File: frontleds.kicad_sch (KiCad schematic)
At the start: 5 parts, among them J13 Conn_02x10_Odd_Even, J5 Conn_02x10_Odd_Even, U18 DMG2305UX-7

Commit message: smol boi
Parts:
- J13, J5: symbol Connector_Generic:Conn_02x10_Counter_Clockwise -> Connector_Generic:Conn_02x10_Odd_Even
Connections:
- net GND: now also J13.1 (Pin_1), J13.3 (Pin_3), J13.5 (Pin_5), J13.7 (Pin_7), J13.9 (Pin_9), J5.11 (Pin_11), J5.13 (Pin_13), J5.15 (Pin_15), J5.17 (Pin_17), J5.19 (Pin_19); no longer J13.12 (Pin_12), J13.14 (Pin_14), J13.16 (Pin_16), J13.18 (Pin_18), J13.20 (Pin_20), J5.10 (Pin_10), J5.2 (Pin_2), J5.4 (Pin_4), J5.6 (Pin_6), J5.8 (Pin_8)
- net LED_1_POW: now also J5.10 (Pin_10), J5.2 (Pin_2), J5.4 (Pin_4), J5.6 (Pin_6), J5.8 (Pin_8); no longer J5.11 (Pin_11), J5.13 (Pin_13), J5.15 (Pin_15), J5.17 (Pin_17), J5.19 (Pin_19)
- net LED_2_POW: now also J13.12 (Pin_12), J13.14 (Pin_14), J13.16 (Pin_16), J13.18 (Pin_18), J13.20 (Pin_20); no longer J13.1 (Pin_1), J13.3 (Pin_3), J13.5 (Pin_5), J13.7 (Pin_7), J13.9 (Pin_9)
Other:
- moved on the sheet: J13

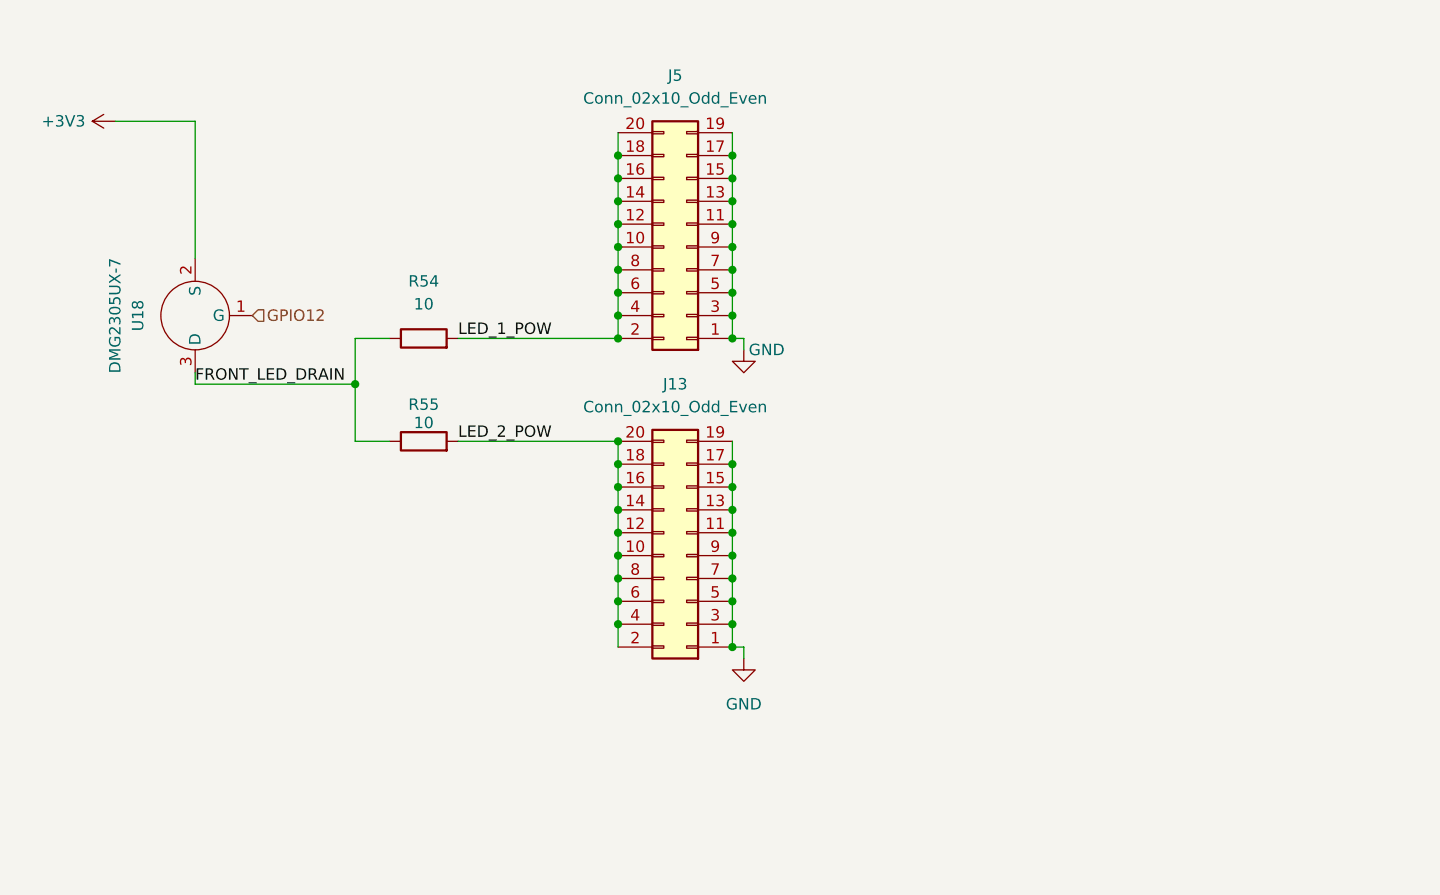
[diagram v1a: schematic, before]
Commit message: changed front leds to use dedicated led current drivers
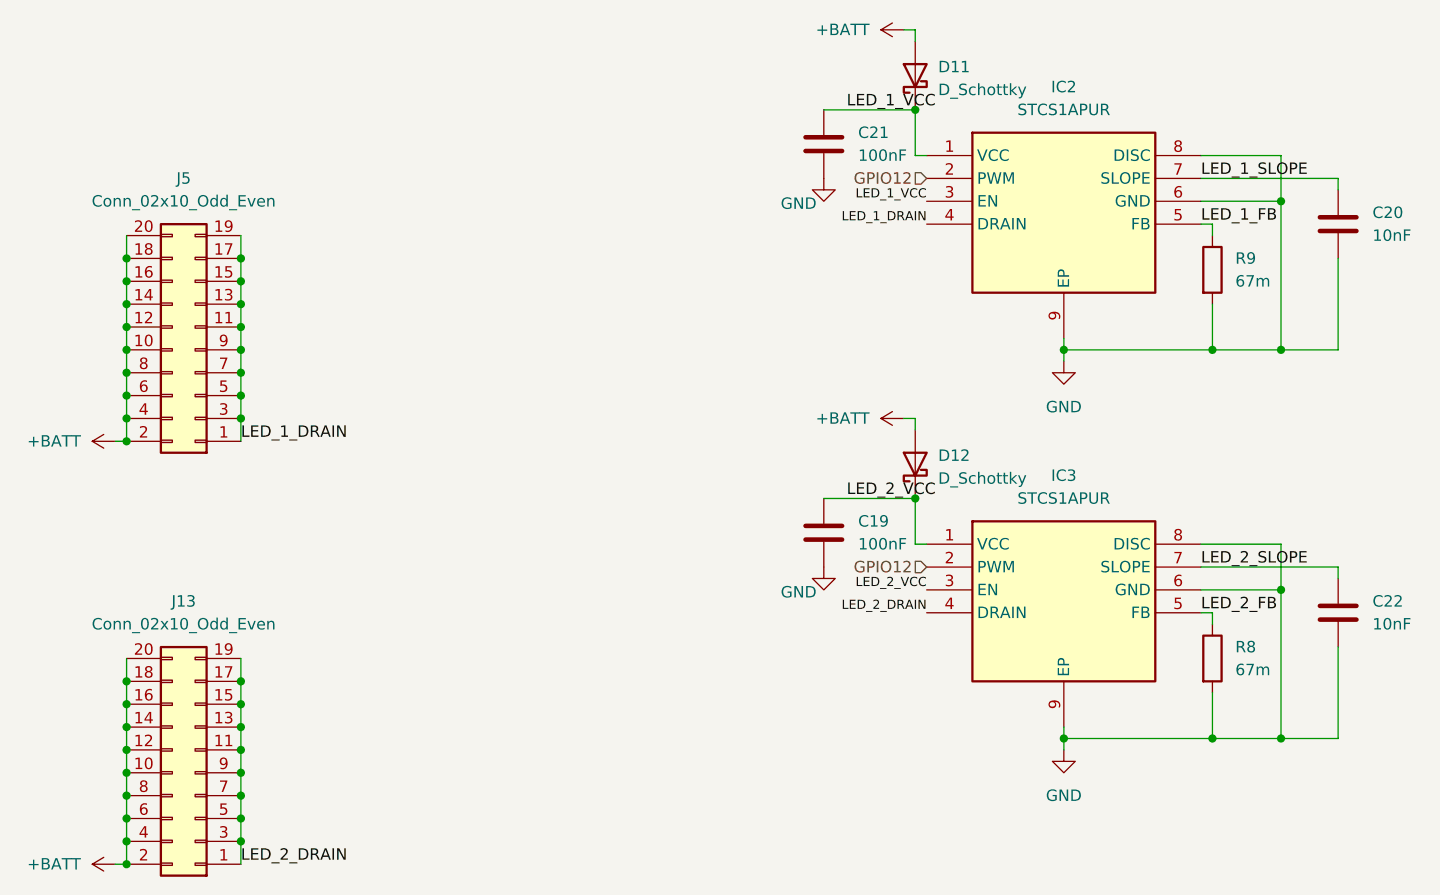
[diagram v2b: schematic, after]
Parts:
- removed R54, R55: 10, Resistor_SMD:R_2512_6332Metric, symbol Device:R
- removed U18: DMG2305UX-7, Package_TO_SOT_SMD:TSOT-23, symbol Transistor_FET:DMG2305UX-7
- added C19, C21: 100nF, Capacitor_SMD:C_0402_1005Metric, symbol Device:C
- added C20, C22: 10nF, Capacitor_SMD:C_0402_1005Metric, symbol Device:C
- added D11, D12: D_Schottky, Diode_SMD:D_SOD-123, symbol Device:D_Schottky
- added IC2, IC3: STCS1APUR, Dry_Lettuce:SON50P300X300X100-9N-D, symbol Dry_Lettuce:STCS1APUR
- added R8, R9: 67m, Resistor_SMD:R_0402_1005Metric, symbol Device:R
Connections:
- net LED_2_POW is gone; now on net +BATT: J13.10 (Pin_10), J13.12 (Pin_12), J13.14 (Pin_14), J13.16 (Pin_16), J13.18 (Pin_18), J13.2 (Pin_2), J13.20 (Pin_20), J13.4 (Pin_4), J13.6 (Pin_6), J13.8 (Pin_8)
- net GND: now also C19.2, C20.2, C21.2, C22.2, IC2.6 (GND), IC2.8 (DISC), IC2.9 (EP), IC3.6 (GND), IC3.8 (DISC), IC3.9 (EP), R8.2, R9.2; no longer J13.1 (Pin_1), J13.11 (Pin_11), J13.13 (Pin_13), J13.15 (Pin_15), J13.17 (Pin_17), J13.19 (Pin_19), J13.3 (Pin_3), J13.5 (Pin_5), J13.7 (Pin_7), J13.9 (Pin_9), J5.1 (Pin_1), J5.11 (Pin_11), J5.13 (Pin_13), J5.15 (Pin_15), J5.17 (Pin_17), J5.19 (Pin_19), J5.3 (Pin_3), J5.5 (Pin_5), J5.7 (Pin_7), J5.9 (Pin_9)
- net GPIO12: now also IC2.2 (PWM), IC3.2 (PWM)
- net LED_1_POW renamed +BATT
- net +BATT: now also D11.2 (A), D12.2 (A)
- new net LED_1_DRAIN: IC2.4 (DRAIN), J5.1 (Pin_1), J5.11 (Pin_11), J5.13 (Pin_13), J5.15 (Pin_15), J5.17 (Pin_17), J5.19 (Pin_19), J5.3 (Pin_3), J5.5 (Pin_5), J5.7 (Pin_7), J5.9 (Pin_9)
- new net LED_1_FB: IC2.5 (FB), R9.1
- new net LED_1_SLOPE: C20.1, IC2.7 (SLOPE)
- new net LED_1_VCC: C21.1, D11.1 (K), IC2.1 (VCC), IC2.3 (EN)
- new net LED_2_DRAIN: IC3.4 (DRAIN), J13.1 (Pin_1), J13.11 (Pin_11), J13.13 (Pin_13), J13.15 (Pin_15), J13.17 (Pin_17), J13.19 (Pin_19), J13.3 (Pin_3), J13.5 (Pin_5), J13.7 (Pin_7), J13.9 (Pin_9)
- new net LED_2_FB: IC3.5 (FB), R8.1
- new net LED_2_SLOPE: C22.1, IC3.7 (SLOPE)
- new net LED_2_VCC: C19.1, D12.1 (K), IC3.1 (VCC), IC3.3 (EN)
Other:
- moved on the sheet: J13, J5

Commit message: tied STCS1A en to pwm
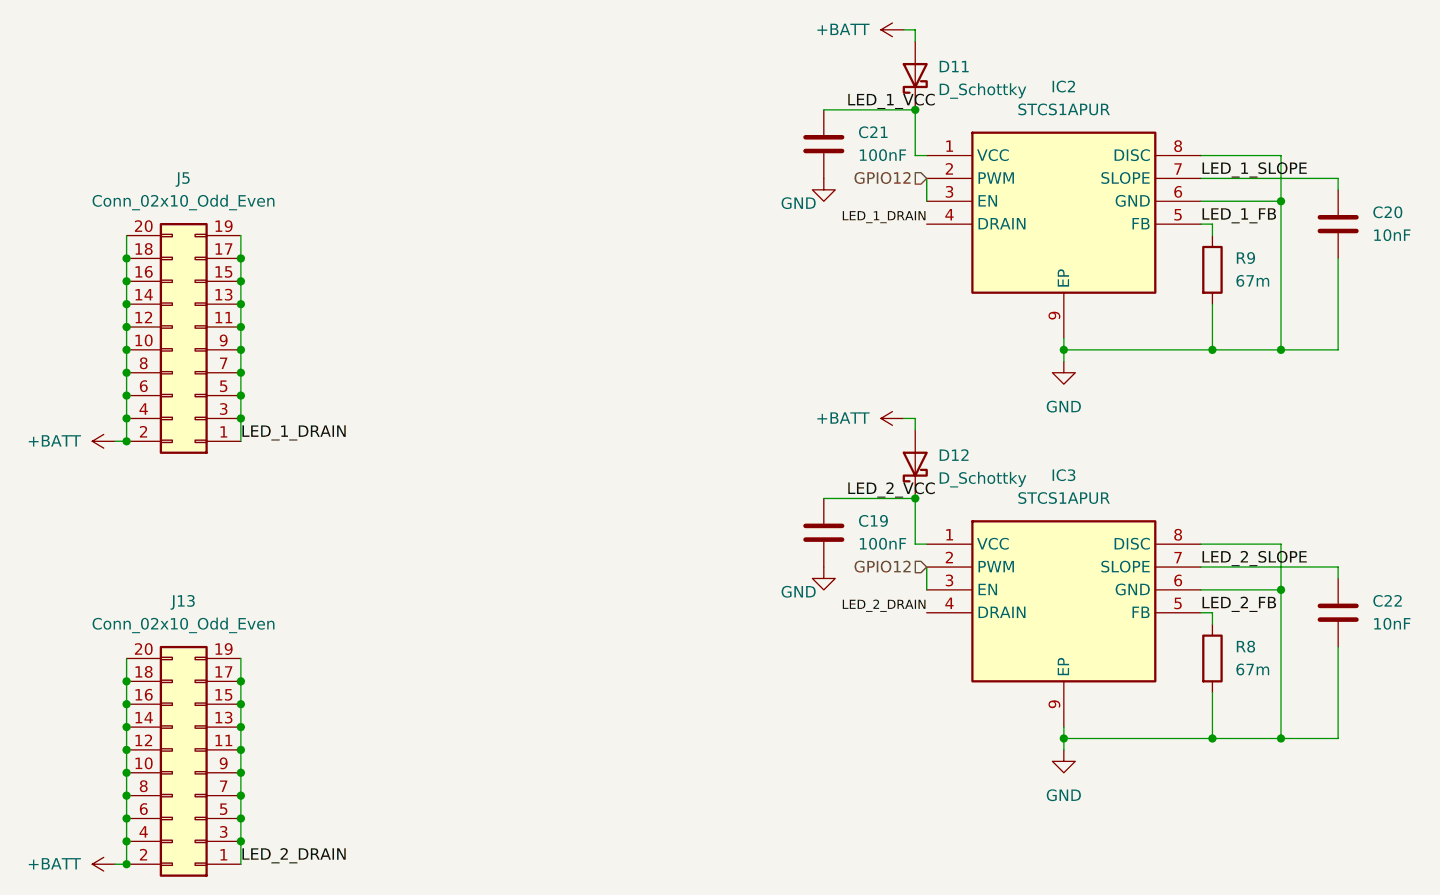
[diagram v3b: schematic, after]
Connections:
- net GPIO12: now also IC2.3 (EN), IC3.3 (EN)
- net LED_1_VCC: no longer IC2.3 (EN)
- net LED_2_VCC: no longer IC3.3 (EN)
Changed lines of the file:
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@@
+	(wire
+		(pts
+			(xy 134.62 31.75) (xy 134.62 34.29)
+		)
+		(stroke
+			(width 0)
+			(type default)
+		)
+	)
 	(wire
 		(pts
@@
 		(pts
 			(xy 58.42 100.33) (xy 58.42 97.79)
+		)
+		(stroke
+			(width 0)
+			(type default)
+		)
+	)
+	(wire
+		(pts
+			(xy 134.62 74.93) (xy 134.62 77.47)
 		)
 		(stroke
@@
 		)
 	)
-	(label "LED_2_VCC"
-		(at 134.62 77.47 180)
-		(effects
-			(font
-				(size 1.016 1.016)
-			)
-			(justify right bottom)
-		)
-	)
 	(label "LED_1_VCC"
 		(at 125.73 24.13 0)
@@
 		)
 	)
-	(label "LED_1_VCC"
-		(at 134.62 34.29 180)
-		(effects
-			(font
-				(size 1.016 1.016)
-			)
-			(justify right bottom)
-		)
-	)

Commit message: export steps
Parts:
- renumbered C21 to C1, C19 to C2, C20 to C3, C22 to C4, D11 to D1, D12 to D2, IC2 to IC1, IC3 to IC2, J5 to J1, J13 to J2, R9 to R1, R8 to R2
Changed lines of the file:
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@@
 		(dnp no)
 		(fields_autoplaced yes)
-		(property "Reference" "#PWR025"
+		(property "Reference" "#PWR05"
 			(at 135.89 15.24 0)
 			(effects
@@
 				)
 			)
+			(project "frontleds"
+				(path "/c5055a52-2a59-4ac7-8e13-bfa74af8a63f"
+					(reference "#PWR05")
+					(unit 1)
+				)
+			)
 		)
 	)
@@
 		(dnp no)
 		(fields_autoplaced yes)
-		(property "Reference" "D12"
+		(property "Reference" "D2"
 			(at 135.89 62.5474 90)
 			(effects
@@
 				)
 			)
+			(project "frontleds"
+				(path "/c5055a52-2a59-4ac7-8e13-bfa74af8a63f"
+					(reference "D2")
+					(unit 1)
+				)
+			)
 		)
 	)
@@
 		(dnp no)
 		(fields_autoplaced yes)
-		(property "Reference" "#PWR027"
+		(property "Reference" "#PWR02"
 			(at 48.26 107.95 0)
 			(effects
@@
 				)
 			)
+			(project "frontleds"
+				(path "/c5055a52-2a59-4ac7-8e13-bfa74af8a63f"
+					(reference "#PWR02")
+					(unit 1)
+				)
+			)
 		)
 	)
@@
 		(dnp no)
 		(fields_autoplaced yes)
-		(property "Reference" "#PWR023"
+		(property "Reference" "#PWR07"
 			(at 149.86 58.42 0)
 			(effects
@@
 				)
 			)
+			(project "frontleds"
+				(path "/c5055a52-2a59-4ac7-8e13-bfa74af8a63f"
+					(reference "#PWR07")
+					(unit 1)
+				)
+			)
 		)
 	)
@@
 		(dnp no)
 		(fields_autoplaced yes)
-		(property "Reference" "R9"
+		(property "Reference" "R1"
 			(at 168.91 40.6399 0)
 			(effects
@@
 				)
 			)
+			(project "frontleds"
+				(path "/c5055a52-2a59-4ac7-8e13-bfa74af8a63f"
+					(reference "R1")
+					(unit 1)
+				)
+			)
 		)
 	)
@@
 		(on_board yes)
 		(dnp no)
-		(property "Reference" "#PWR026"
+		(property "Reference" "#PWR03"
 			(at 123.19 38.1 0)
 			(effects
@@
 				)
 			)
+			(project "frontleds"
+				(path "/c5055a52-2a59-4ac7-8e13-bfa74af8a63f"
+					(reference "#PWR03")
+					(unit 1)
+				)
+			)
 		)
 	)
@@
 		(dnp no)
 		(fields_autoplaced yes)
-		(property "Reference" "J13"
+		(property "Reference" "J2"
 			(at 52.07 78.74 0)
 			(effects
@@
 				)
 			)
+			(project "frontleds"
+				(path "/c5055a52-2a59-4ac7-8e13-bfa74af8a63f"
+					(reference "J2")
+					(unit 1)
+				)
+			)
 		)
 	)
@@
 		(dnp no)
 		(fields_autoplaced yes)
-		(property "Reference" "IC3"
+		(property "Reference" "IC2"
 			(at 149.86 64.77 0)
 			(effects
@@
 				)
 			)
+			(project "frontleds"
+				(path "/c5055a52-2a59-4ac7-8e13-bfa74af8a63f"
+					(reference "IC2")
+					(unit 1)
+				)
+			)
 		)
 	)
@@
 		(dnp no)
 		(fields_autoplaced yes)
-		(property "Reference" "IC2"
+		(property "Reference" "IC1"
 			(at 149.86 21.59 0)
 			(effects
@@
 				)
 			)
+			(project "frontleds"
+				(path "/c5055a52-2a59-4ac7-8e13-bfa74af8a63f"
+					(reference "IC1")
+					(unit 1)
+				)
+			)
 		)
 	)
@@
 		(dnp no)
 		(fields_autoplaced yes)
-		(property "Reference" "C20"
+		(property "Reference" "C3"
 			(at 184.15 35.5599 0)
 			(effects
@@
 				)
 			)
+			(project "frontleds"
+				(path "/c5055a52-2a59-4ac7-8e13-bfa74af8a63f"
+					(reference "C3")
+					(unit 1)
+				)
+			)
 		)
 	)
@@
 		(dnp no)
 		(fields_autoplaced yes)
-		(property "Reference" "C19"
+		(property "Reference" "C2"
 			(at 127 69.8499 0)
 			(effects
@@
 				)
 			)
+			(project "frontleds"
+				(path "/c5055a52-2a59-4ac7-8e13-bfa74af8a63f"
+					(reference "C2")
+					(unit 1)
+				)
+			)
 		)
 	)
@@
 		(dnp no)
 		(fields_autoplaced yes)
-		(property "Reference" "C22"
+		(property "Reference" "C4"
 			(at 184.15 78.7399 0)
 			(effects
@@
 				)
 			)
+			(project "frontleds"
+				(path "/c5055a52-2a59-4ac7-8e13-bfa74af8a63f"
+					(reference "C4")
+					(unit 1)
+				)
+			)
 		)
 	)
@@
 		(on_board yes)
 		(dnp no)
-		(property "Reference" "#PWR021"
+		(property "Reference" "#PWR04"
 			(at 123.19 81.28 0)
 			(effects
@@
 				)
 			)
+			(project "frontleds"
+				(path "/c5055a52-2a59-4ac7-8e13-bfa74af8a63f"
+					(reference "#PWR04")
+					(unit 1)
+				)
+			)
 		)
 	)
@@
 		(dnp no)
 		(fields_autoplaced yes)
-		(property "Reference" "#PWR024"
+		(property "Reference" "#PWR08"
 			(at 149.86 101.6 0)
 			(effects
@@
 				)
 			)
+			(project "frontleds"
+				(path "/c5055a52-2a59-4ac7-8e13-bfa74af8a63f"
+					(reference "#PWR08")
+					(unit 1)
+				)
+			)
 		)
 	)
@@
 		(dnp no)
 		(fields_autoplaced yes)
-		(property "Reference" "D11"
+		(property "Reference" "D1"
 			(at 135.89 19.3674 90)
 			(effects
@@
 				)
 			)
+			(project "frontleds"
+				(path "/c5055a52-2a59-4ac7-8e13-bfa74af8a63f"
+					(reference "D1")
+					(unit 1)
+				)
+			)
 		)
 	)
@@
 		(dnp no)
 		(fields_autoplaced yes)
-		(property "Reference" "C21"
+		(property "Reference" "C1"
 			(at 127 26.6699 0)
 			(effects
@@
 				)
 			)
+			(project "frontleds"
+				(path "/c5055a52-2a59-4ac7-8e13-bfa74af8a63f"
+					(reference "C1")
+					(unit 1)
+				)
+			)
 		)
 	)
@@
 		(dnp no)
 		(fields_autoplaced yes)
-		(property "Reference" "#PWR022"
+		(property "Reference" "#PWR06"
 			(at 135.89 58.42 0)
 			(effects
@@
 				)
 			)
+			(project "frontleds"
+				(path "/c5055a52-2a59-4ac7-8e13-bfa74af8a63f"
+					(reference "#PWR06")
+					(unit 1)
+				)
+			)
 		)
 	)
@@
 		(dnp no)
 		(fields_autoplaced yes)
-		(property "Reference" "#PWR020"
+		(property "Reference" "#PWR01"
 			(at 48.26 60.96 0)
 			(effects
@@
 				)
 			)
+			(project "frontleds"
+				(path "/c5055a52-2a59-4ac7-8e13-bfa74af8a63f"
+					(reference "#PWR01")
+					(unit 1)
+				)
+			)
 		)
 	)
@@
 		(dnp no)
 		(fields_autoplaced yes)
-		(property "Reference" "R8"
+		(property "Reference" "R2"
 			(at 168.91 83.8199 0)
 			(effects
@@
 				)
 			)
+			(project "frontleds"
+				(path "/c5055a52-2a59-4ac7-8e13-bfa74af8a63f"
+					(reference "R2")
+					(unit 1)
+				)
+			)
 		)
 	)
@@
 		(dnp no)
 		(fields_autoplaced yes)
-		(property "Reference" "J5"
+		(property "Reference" "J1"
 			(at 52.07 31.75 0)
 			(effects
@@
 				)
 			)
-		)
-	)
+			(project "frontleds"
+				(path "/c5055a52-2a59-4ac7-8e13-bfa74af8a63f"
+					(reference "J1")
+					(unit 1)
+				)
+			)
+		)
+	)
+	(sheet_instances
+		(path "/"
+			(page "1")
+		)
+	)
+	(embedded_fonts no)
 )
